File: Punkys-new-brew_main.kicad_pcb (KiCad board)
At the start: 2 copper layers, 40.1 x 110 mm, 41 parts, among them J1 +12v, J11 1x10_main, J13 L_1x12_main, J16 R_1x12_main, U1 LM556, U2 TL074, U3 VTL5C

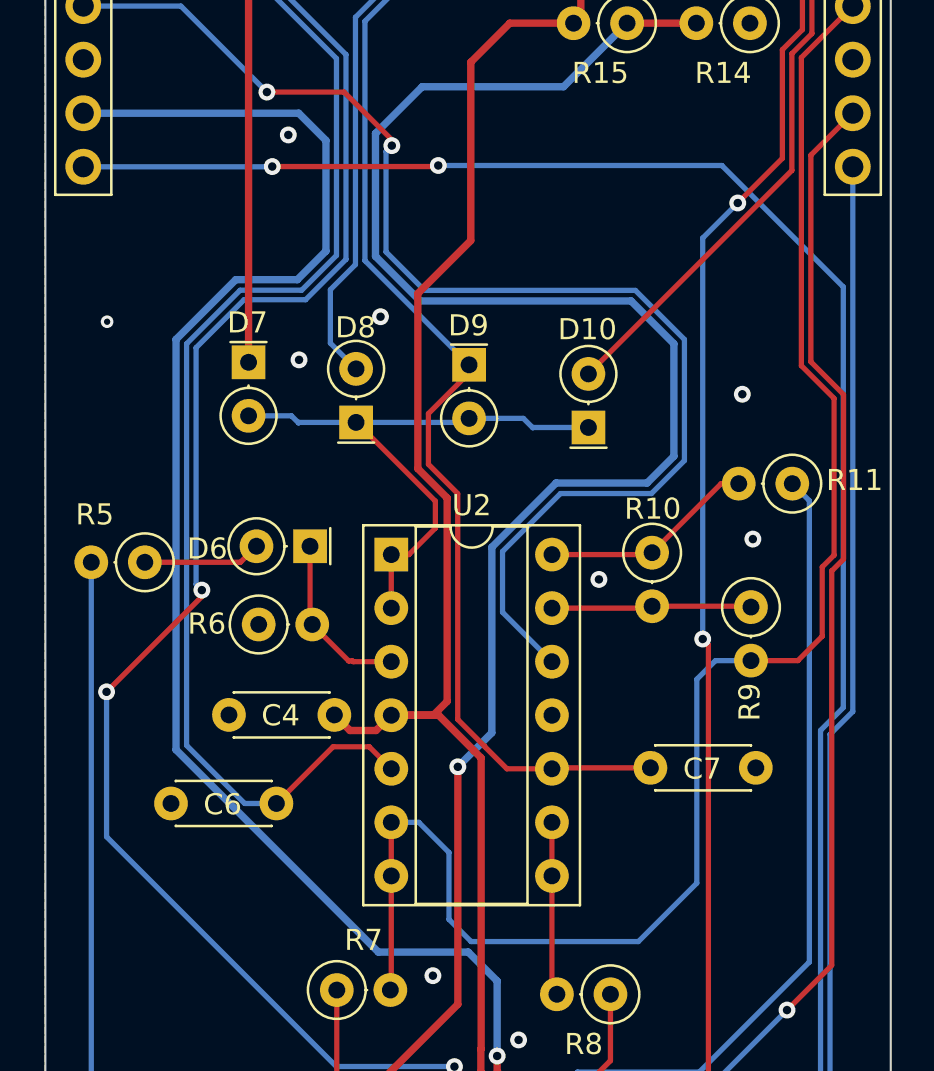
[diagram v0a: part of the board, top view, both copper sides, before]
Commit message: fixed some values to better suit my liking. re-routed the invert to env2 instead, it works better me finks.
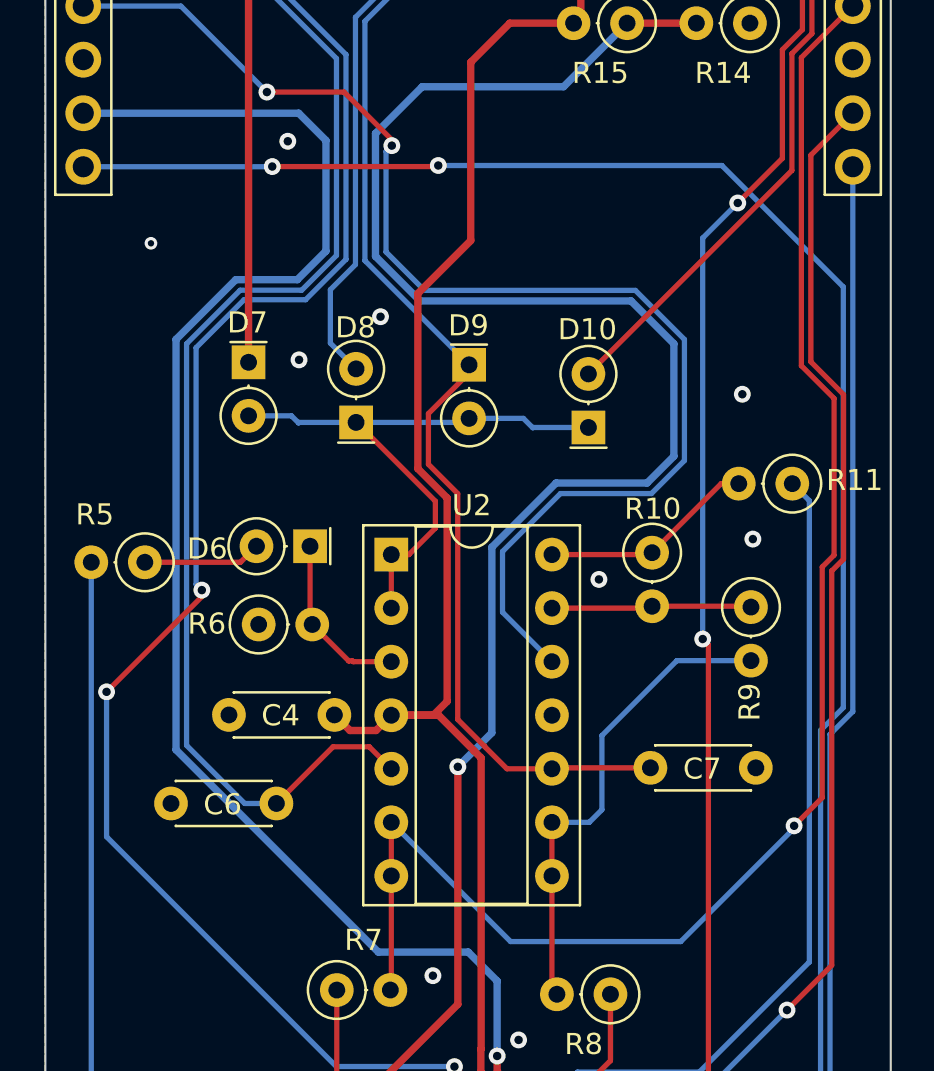
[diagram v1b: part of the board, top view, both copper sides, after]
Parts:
- C3: value 100nF -> 47nF
- C4, C5: value 10nF -> 100nF
- C6, C7: value 2.2uF -> 1uF
- R2, R4: value 100k -> 1k
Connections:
- R9 pad 2: ENV1 -> Net-(U2C--)
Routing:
- net Net-(U2C--): track 8.25 -> 22.9 mm
- net ENV1: track 76.1 -> 73.1 mm, vias 0 -> 1
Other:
- board text added: "-NEW-"
